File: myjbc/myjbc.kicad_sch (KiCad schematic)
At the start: 1 part

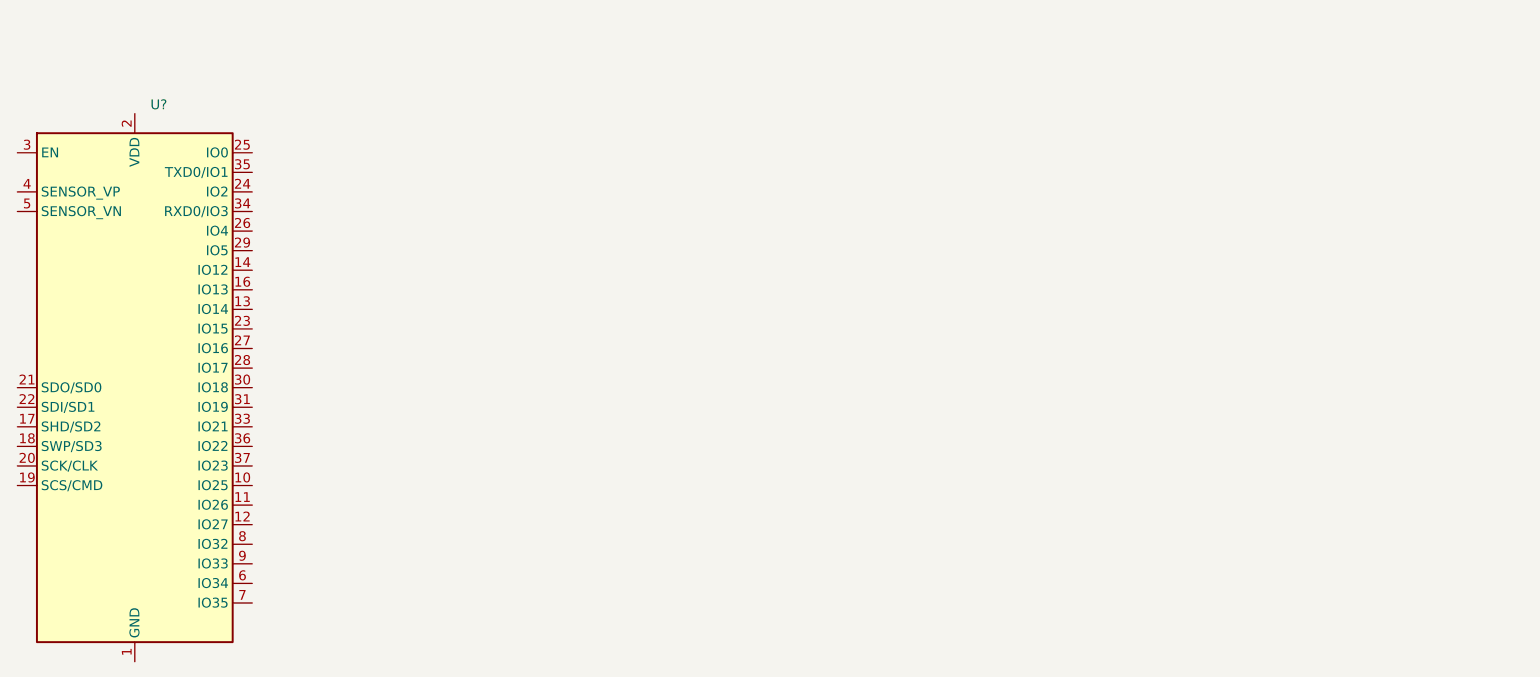
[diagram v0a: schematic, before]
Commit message: Current measurment
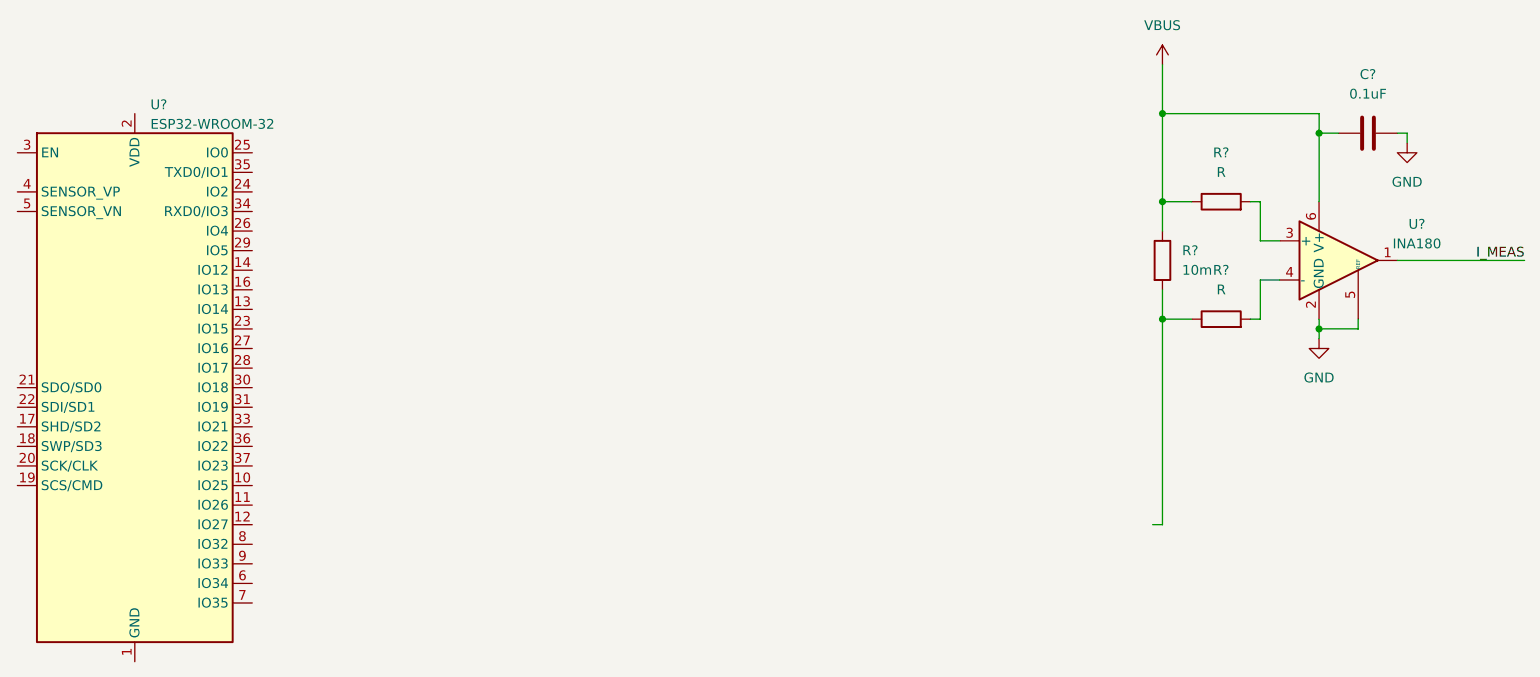
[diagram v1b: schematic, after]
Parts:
- added C?: 0.1uF, symbol Device:C
- added R? (x2): R, symbol Device:R
- added R?: 10m, symbol Device:R
- added U?: INA180, Package_TO_SOT_SMD:SOT-23-6, symbol Amplifier_Current:INA181
- U?: value (none) -> ESP32-WROOM-32; footprint (none) -> RF_Module:ESP32-WROOM-32
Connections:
- new net: R?.1, R?.2
- new net: R?.2, U?.4 (-)
- new net: R?.2, U?.3 (+)
- new net GND: C?.2, U?.2 (GND), U?.5 (REF)
- new net I_MEAS: U?.1
- new net VBUS: C?.1, R?.1, R?.1, U?.6 (V+)
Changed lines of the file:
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@@
 (kicad_sch (version 20211123) (generator eeschema)
   (paper "A4")
+  (junction (at 215.9 43.18) (diameter 0) (color 0 0 0 0)
+  )
+  (junction (at 195.58 52.07) (diameter 0) (color 0 0 0 0)
+  )
+  (junction (at 195.58 67.31) (diameter 0) (color 0 0 0 0)
+  )
+  (junction (at 195.58 40.64) (diameter 0) (color 0 0 0 0)
+  )
+  (junction (at 215.9 68.58) (diameter 0) (color 0 0 0 0)
+  )
+  (wire (pts (xy 195.58 52.07) (xy 199.39 52.07))
+    (stroke (width 0) (type default) (color 0 0 0 0))
+  )
+  (wire (pts (xy 215.9 68.58) (xy 215.9 69.85))
+    (stroke (width 0) (type default) (color 0 0 0 0))
+  )
+  (wire (pts (xy 194.31 93.98) (xy 195.58 93.98))
+    (stroke (width 0) (type default) (color 0 0 0 0))
+  )
+  (wire (pts (xy 207.01 67.31) (xy 208.28 67.31))
+    (stroke (width 0) (type default) (color 0 0 0 0))
+  )
+  (wire (pts (xy 215.9 43.18) (xy 215.9 40.64))
+    (stroke (width 0) (type default) (color 0 0 0 0))
+  )
+  (wire (pts (xy 195.58 55.88) (xy 195.58 52.07))
+    (stroke (width 0) (type default) (color 0 0 0 0))
+  )
+  (wire (pts (xy 227.33 44.45) (xy 227.33 43.18))
+    (stroke (width 0) (type default) (color 0 0 0 0))
+  )
+  (wire (pts (xy 226.06 59.69) (xy 242.57 59.69))
+    (stroke (width 0) (type default) (color 0 0 0 0))
+  )
+  (wire (pts (xy 195.58 40.64) (xy 215.9 40.64))
+    (stroke (width 0) (type default) (color 0 0 0 0))
+  )
+  (wire (pts (xy 215.9 68.58) (xy 220.98 68.58))
+    (stroke (width 0) (type default) (color 0 0 0 0))
+  )
+  (wire (pts (xy 208.28 52.07) (xy 208.28 57.15))
+    (stroke (width 0) (type default) (color 0 0 0 0))
+  )
+  (wire (pts (xy 215.9 67.31) (xy 215.9 68.58))
+    (stroke (width 0) (type default) (color 0 0 0 0))
+  )
+  (wire (pts (xy 215.9 43.18) (xy 215.9 52.07))
+    (stroke (width 0) (type default) (color 0 0 0 0))
+  )
+  (wire (pts (xy 215.9 43.18) (xy 218.44 43.18))
+    (stroke (width 0) (type default) (color 0 0 0 0))
+  )
+  (wire (pts (xy 199.39 67.31) (xy 195.58 67.31))
+    (stroke (width 0) (type default) (color 0 0 0 0))
+  )
+  (wire (pts (xy 207.01 52.07) (xy 208.28 52.07))
+    (stroke (width 0) (type default) (color 0 0 0 0))
+  )
+  (wire (pts (xy 195.58 34.29) (xy 195.58 40.64))
+    (stroke (width 0) (type default) (color 0 0 0 0))
+  )
+  (wire (pts (xy 208.28 62.23) (xy 210.82 62.23))
+    (stroke (width 0) (type default) (color 0 0 0 0))
+  )
+  (wire (pts (xy 195.58 67.31) (xy 195.58 93.98))
+    (stroke (width 0) (type default) (color 0 0 0 0))
+  )
+  (wire (pts (xy 208.28 57.15) (xy 210.82 57.15))
+    (stroke (width 0) (type default) (color 0 0 0 0))
+  )
+  (wire (pts (xy 195.58 67.31) (xy 195.58 63.5))
+    (stroke (width 0) (type default) (color 0 0 0 0))
+  )
+  (wire (pts (xy 220.98 68.58) (xy 220.98 67.31))
+    (stroke (width 0) (type default) (color 0 0 0 0))
+  )
+  (wire (pts (xy 208.28 67.31) (xy 208.28 62.23))
+    (stroke (width 0) (type default) (color 0 0 0 0))
+  )
+  (wire (pts (xy 195.58 40.64) (xy 195.58 52.07))
+    (stroke (width 0) (type default) (color 0 0 0 0))
+  )
+  (wire (pts (xy 227.33 43.18) (xy 226.06 43.18))
+    (stroke (width 0) (type default) (color 0 0 0 0))
+  )
+  (label "I_MEAS" (at 242.57 59.69 180)
+    (effects (font (size 1.27 1.27)) (justify right bottom))
+  )
+  (symbol (lib_id "Device:R") (at 203.2 67.31 90) (unit 1)
+    (in_bom yes) (on_board yes) (fields_autoplaced)
+    (property "Reference" "R?" (id 0) (at 203.2 60.96 90))
+    (property "Value" "R" (id 1) (at 203.2 63.5 90))
+    (property "Footprint" "" (id 2) (at 203.2 69.088 90)
+      (effects (font (size 1.27 1.27)) hide)
+    )
+    (property "Datasheet" "~" (id 3) (at 203.2 67.31 0)
+      (effects (font (size 1.27 1.27)) hide)
+    )
+    (pin "1")
+    (pin "2")
+  )
+  (symbol (lib_id "Amplifier_Current:INA181") (at 218.44 59.69 0) (unit 1)
+    (in_bom yes) (on_board yes) (fields_autoplaced)
+    (property "Reference" "U?" (id 0) (at 228.6 54.991 0))
+    (property "Value" "INA180" (id 1) (at 228.6 57.531 0))
+    (property "Footprint" "Package_TO_SOT_SMD:SOT-23-6" (id 2) (at 219.71 58.42 0)
+      (effects (font (size 1.27 1.27)) hide)
+    )
+    (property "Datasheet" "http://www.ti.com/lit/ds/symlink/ina181.pdf" (id 3) (at 222.25 55.88 0)
+      (effects (font (size 1.27 1.27)) hide)
+    )
+    (pin "1")
+    (pin "2")
+    (pin "3")
+    (pin "4")
+    (pin "5")
+    (pin "6")
+  )
+  (symbol (lib_id "power:VBUS") (at 195.58 34.29 0) (unit 1)
+    (in_bom yes) (on_board yes) (fields_autoplaced)
+    (property "Reference" "#PWR?" (id 0) (at 195.58 38.1 0)
+      (effects (font (size 1.27 1.27)) hide)
+    )
+    (property "Value" "VBUS" (id 1) (at 195.58 29.21 0))
+    (property "Footprint" "" (id 2) (at 195.58 34.29 0)
+      (effects (font (size 1.27 1.27)) hide)
+    )
+    (property "Datasheet" "" (id 3) (at 195.58 34.29 0)
+      (effects (font (size 1.27 1.27)) hide)
+    )
+    (pin "1")
+  )
+  (symbol (lib_id "Device:R") (at 195.58 59.69 0) (unit 1)
+    (in_bom yes) (on_board yes) (fields_autoplaced)
+    (property "Reference" "R?" (id 0) (at 198.12 58.4199 0)
+      (effects (font (size 1.27 1.27)) (justify left))
+    )
+    (property "Value" "10m" (id 1) (at 198.12 60.9599 0)
+      (effects (font (size 1.27 1.27)) (justify left))
+    )
+    (property "Footprint" "" (id 2) (at 193.802 59.69 90)
+      (effects (font (size 1.27 1.27)) hide)
+    )
+    (property "Datasheet" "~" (id 3) (at 195.58 59.69 0)
+      (effects (font (size 1.27 1.27)) hide)
+    )
+    (pin "1")
+    (pin "2")
+  )
+  (symbol (lib_id "power:GND") (at 215.9 69.85 0) (unit 1)
+    (in_bom yes) (on_board yes) (fields_autoplaced)
+    (property "Reference" "#PWR?" (id 0) (at 215.9 76.2 0)
+      (effects (font (size 1.27 1.27)) hide)
+    )
+    (property "Value" "GND" (id 1) (at 215.9 74.93 0))
+    (property "Footprint" "" (id 2) (at 215.9 69.85 0)
+      (effects (font (size 1.27 1.27)) hide)
+    )
+    (property "Datasheet" "" (id 3) (at 215.9 69.85 0)
+      (effects (font (size 1.27 1.27)) hide)
+    )
+    (pin "1")
+  )
+  (symbol (lib_id "Device:R") (at 203.2 52.07 90) (unit 1)
+    (in_bom yes) (on_board yes) (fields_autoplaced)
+    (property "Reference" "R?" (id 0) (at 203.2 45.72 90))
+    (property "Value" "R" (id 1) (at 203.2 48.26 90))
+    (property "Footprint" "" (id 2) (at 203.2 53.848 90)
+      (effects (font (size 1.27 1.27)) hide)
+    )
+    (property "Datasheet" "~" (id 3) (at 203.2 52.07 0)
+      (effects (font (size 1.27 1.27)) hide)
+    )
+    (pin "1")
+    (pin "2")
+  )
+  (symbol (lib_id "Device:C") (at 222.25 43.18 90) (unit 1)
+    (in_bom yes) (on_board yes) (fields_autoplaced)
+    (property "Reference" "C?" (id 0) (at 222.25 35.56 90))
+    (property "Value" "0.1uF" (id 1) (at 222.25 38.1 90))
+    (property "Footprint" "" (id 2) (at 226.06 42.2148 0)
+      (effects (font (size 1.27 1.27)) hide)
+    )
+    (property "Datasheet" "~" (id 3) (at 222.25 43.18 0)
+      (effects (font (size 1.27 1.27)) hide)
+    )
+    (pin "1")
+    (pin "2")
+  )
   (symbol (lib_id "RF_Module:ESP32-WROOM-32") (at 62.23 76.2 0) (unit 1)
     (in_bom yes) (on_board yes) (fields_autoplaced)
@@
       (effects (font (size 1.27 1.27)) (justify left))
     )
-    (property "Value" "" (id 1) (at 64.2494 42.0171 0)
-      (effects (font (size 1.27 1.27)) (justify left))
-    )
-    (property "Footprint" "" (id 2) (at 62.23 114.3 0)
+    (property "Value" "ESP32-WROOM-32" (id 1) (at 64.2494 42.0171 0)
+      (effects (font (size 1.27 1.27)) (justify left))
+    )
+    (property "Footprint" "RF_Module:ESP32-WROOM-32" (id 2) (at 62.23 114.3 0)
       (effects (font (size 1.27 1.27)) hide)
     )
@@
     (pin "9")
   )
+  (symbol (lib_id "power:GND") (at 227.33 44.45 0) (unit 1)
+    (in_bom yes) (on_board yes) (fields_autoplaced)
+    (property "Reference" "#PWR?" (id 0) (at 227.33 50.8 0)
+      (effects (font (size 1.27 1.27)) hide)
+    )
+    (property "Value" "GND" (id 1) (at 227.33 49.53 0))
+    (property "Footprint" "" (id 2) (at 227.33 44.45 0)
+      (effects (font (size 1.27 1.27)) hide)
+    )
+    (property "Datasheet" "" (id 3) (at 227.33 44.45 0)
+      (effects (font (size 1.27 1.27)) hide)
+    )
+    (pin "1")
+  )
   (sheet_instances
     (path "/" (page "1"))
   )
   (symbol_instances
+    (path "/5d9bbed4-bcb3-4ad4-b04e-24b788bf32f7"
+      (reference "#PWR?") (unit 1) (value "VBUS") (footprint "")
+    )
+    (path "/79aa8587-dd14-4562-b209-7fe7e2341e1b"
+      (reference "#PWR?") (unit 1) (value "GND") (footprint "")
+    )
+    (path "/f9d52ea2-de3d-4b16-a251-d5e42189425d"
+      (reference "#PWR?") (unit 1) (value "GND") (footprint "")
+    )
+    (path "/b8c3fbc9-667d-4da1-b0da-a3723287a4c1"
+      (reference "C?") (unit 1) (value "0.1uF") (footprint "")
+    )
+    (path "/10731a38-902e-476b-ae21-755798fcd310"
+      (reference "R?") (unit 1) (value "R") (footprint "")
+    )
+    (path "/73c1eee2-05c6-471c-a3e5-93be837b155c"
+      (reference "R?") (unit 1) (value "10m") (footprint "")
+    )
+    (path "/8e42b90d-a0d0-4cf3-aa87-0f7225fad40f"
+      (reference "R?") (unit 1) (value "R") (footprint "")
+    )
+    (path "/224768bc-6009-43ba-aa4a-70cbaa15b5a3"
+      (reference "U?") (unit 1) (value "INA180") (footprint "Package_TO_SOT_SMD:SOT-23-6")
+    )
     (path "/f0df1061-3eab-4030-9984-4e4c269245fe"
       (reference "U?") (unit 1) (value "ESP32-WROOM-32") (footprint "RF_Module:ESP32-WROOM-32")
